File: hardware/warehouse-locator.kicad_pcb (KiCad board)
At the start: 2 copper layers, 8 parts, among them J1 Screw_Terminal_01x03, J2 Screw_Terminal_01x03, J3 Screw_Terminal_01x03, J4 Barrel_Jack, J5 Screw_Terminal_01x03, J6 Screw_Terminal_01x03, J7 Screw_Terminal_01x03, U1 ESP32-DevKitC

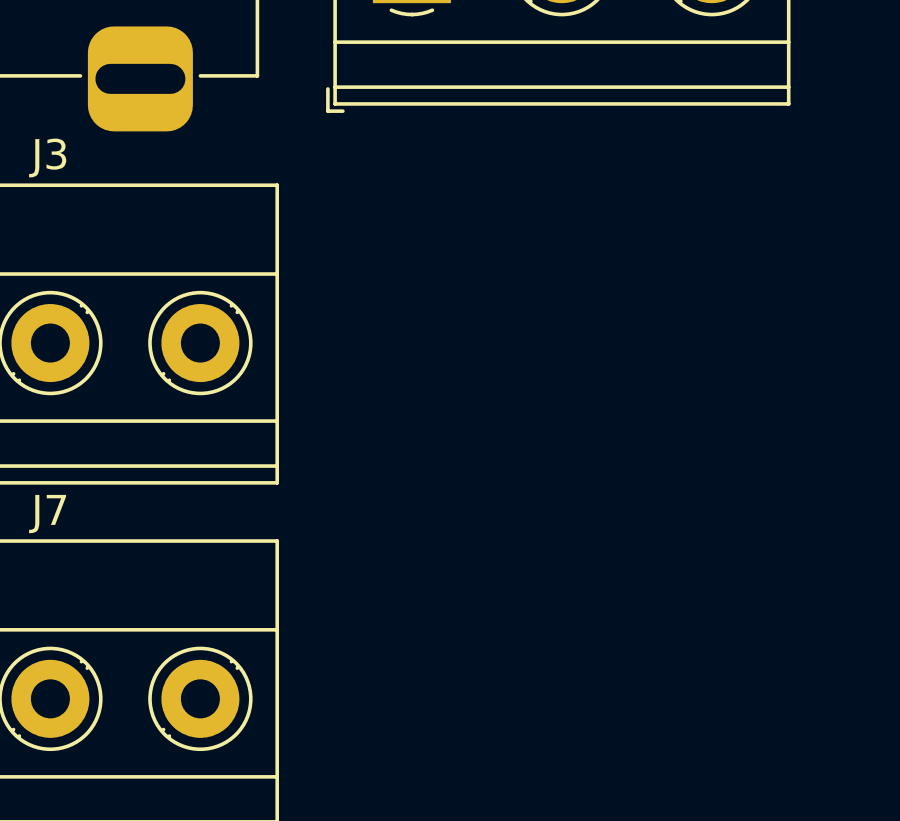
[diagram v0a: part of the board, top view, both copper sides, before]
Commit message: Ethernet header
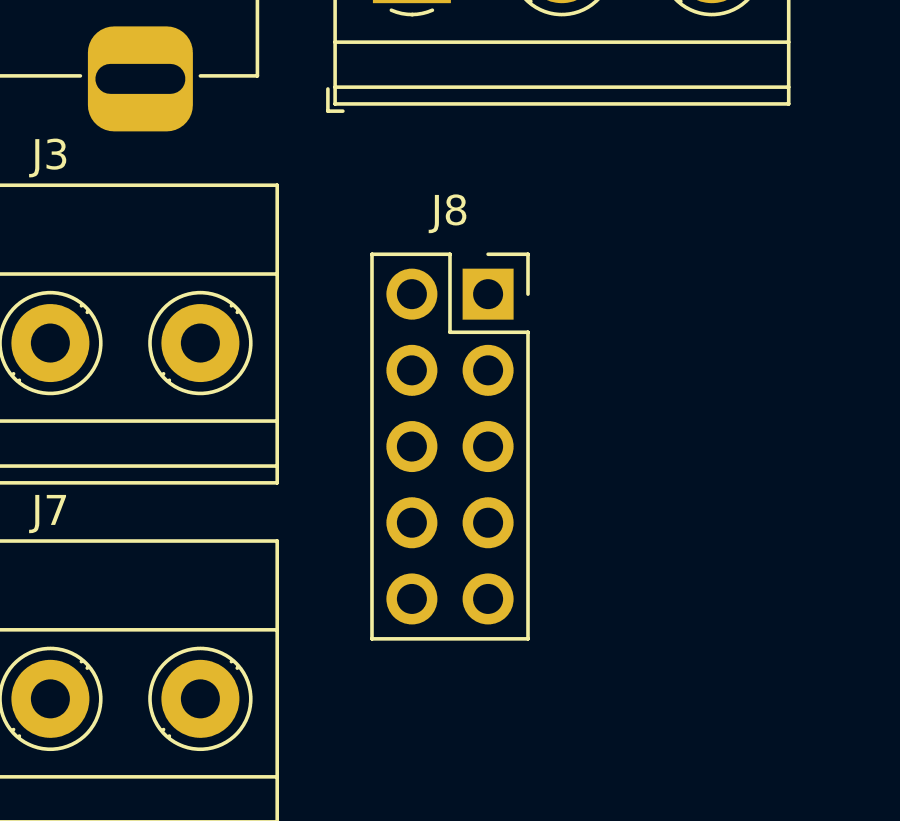
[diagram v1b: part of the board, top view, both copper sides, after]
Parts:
- added J8: Ethernet, Connector_PinSocket_2.54mm:PinSocket_2x05_P2.54mm_Vertical, F.Cu at (170.2, 86.4)
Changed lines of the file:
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@@
   (net 45 "unconnected-(U1-Pad37)")
   (net 46 "unconnected-(U1-Pad38)")
+  (net 47 "unconnected-(J8-Pad1)")
+  (net 48 "unconnected-(J8-Pad2)")
+  (net 49 "unconnected-(J8-Pad3)")
+  (net 50 "/CIPO")
+  (net 51 "/COPI")
+  (net 52 "/SCLK")
+  (net 53 "/ETH_CS")
+  (net 54 "/ETH_RESET")
+  (net 55 "+3.3V")
   (footprint "Espressif:ESP32-DevKitC" (layer "F.Cu")
     (at 119.605 64.83812)
@@
       (offset (xyz 0 0 0))
       (scale (xyz 1 1 1))
+      (rotate (xyz 0 0 0))
+    )
+  )
+  (footprint "Connector_PinSocket_2.54mm:PinSocket_2x05_P2.54mm_Vertical" (layer "F.Cu")
+    (at 170.18 86.36)
+    (descr "Through hole straight socket strip, 2x05, 2.54mm pitch, double cols (from Kicad 4.0.7), script generated")
+    (tags "Through hole socket strip THT 2x05 2.54mm double row")
+    (property "Sheetfile" "warehouse-locator.kicad_sch")
+    (property "Sheetname" "")
+    (attr through_hole)
+    (fp_text reference "J8" (at -1.27 -2.77) (layer "F.SilkS")
+      (effects (font (size 1 1) (thickness 0.15)))
+    )
+    (fp_text value "Ethernet" (at -1.27 12.93) (layer "F.Fab")
+      (effects (font (size 1 1) (thickness 0.15)))
+    )
+    (fp_text user "${REFERENCE}" (at -1.27 5.08 90) (layer "F.Fab")
+      (effects (font (size 1 1) (thickness 0.15)))
+    )
+    (fp_line (start 0 -1.33) (end 1.33 -1.33) (layer "F.SilkS") (width 0.12))
+    (fp_line (start -1.27 1.27) (end 1.33 1.27) (layer "F.SilkS") (width 0.12))
+    (fp_line (start 1.33 1.27) (end 1.33 11.49) (layer "F.SilkS") (width 0.12))
+    (fp_line (start -3.87 -1.33) (end -1.27 -1.33) (layer "F.SilkS") (width 0.12))
+    (fp_line (start -3.87 11.49) (end 1.33 11.49) (layer "F.SilkS") (width 0.12))
+    (fp_line (start -3.87 -1.33) (end -3.87 11.49) (layer "F.SilkS") (width 0.12))
+    (fp_line (start -1.27 -1.33) (end -1.27 1.27) (layer "F.SilkS") (width 0.12))
+    (fp_line (start 1.33 -1.33) (end 1.33 0) (layer "F.SilkS") (width 0.12))
+    (fp_line (start 1.76 -1.8) (end 1.76 11.9) (layer "F.CrtYd") (width 0.05))
+    (fp_line (start 1.76 11.9) (end -4.34 11.9) (layer "F.CrtYd") (width 0.05))
+    (fp_line (start -4.34 11.9) (end -4.34 -1.8) (layer "F.CrtYd") (width 0.05))
+    (fp_line (start -4.34 -1.8) (end 1.76 -1.8) (layer "F.CrtYd") (width 0.05))
+    (fp_line (start -3.81 -1.27) (end 0.27 -1.27) (layer "F.Fab") (width 0.1))
+    (fp_line (start 1.27 11.43) (end -3.81 11.43) (layer "F.Fab") (width 0.1))
+    (fp_line (start 1.27 -0.27) (end 1.27 11.43) (layer "F.Fab") (width 0.1))
+    (fp_line (start -3.81 11.43) (end -3.81 -1.27) (layer "F.Fab") (width 0.1))
+    (fp_line (start 0.27 -1.27) (end 1.27 -0.27) (layer "F.Fab") (width 0.1))
+    (pad "1" thru_hole rect (at 0 0) (size 1.7 1.7) (drill 1) (layers *.Cu *.Mask)
+      (net 47 "unconnected-(J8-Pad1)") (pinfunction "Pin_1") (pintype "passive+no_connect"))
+    (pad "2" thru_hole oval (at -2.54 0) (size 1.7 1.7) (drill 1) (layers *.Cu *.Mask)
+      (net 48 "unconnected-(J8-Pad2)") (pinfunction "Pin_2") (pintype "passive+no_connect"))
+    (pad "3" thru_hole oval (at 0 2.54) (size 1.7 1.7) (drill 1) (layers *.Cu *.Mask)
+      (net 49 "unconnected-(J8-Pad3)") (pinfunction "Pin_3") (pintype "passive+no_connect"))
+    (pad "4" thru_hole oval (at -2.54 2.54) (size 1.7 1.7) (drill 1) (layers *.Cu *.Mask)
+      (net 50 "/CIPO") (pinfunction "Pin_4") (pintype "passive"))
+    (pad "5" thru_hole oval (at 0 5.08) (size 1.7 1.7) (drill 1) (layers *.Cu *.Mask)
+      (net 51 "/COPI") (pinfunction "Pin_5") (pintype "passive"))
+    (pad "6" thru_hole oval (at -2.54 5.08) (size 1.7 1.7) (drill 1) (layers *.Cu *.Mask)
+      (net 52 "/SCLK") (pinfunction "Pin_6") (pintype "passive"))
+    (pad "7" thru_hole oval (at 0 7.62) (size 1.7 1.7) (drill 1) (layers *.Cu *.Mask)
+      (net 53 "/ETH_CS") (pinfunction "Pin_7") (pintype "passive"))
+    (pad "8" thru_hole oval (at -2.54 7.62) (size 1.7 1.7) (drill 1) (layers *.Cu *.Mask)
+      (net 54 "/ETH_RESET") (pinfunction "Pin_8") (pintype "passive"))
+    (pad "9" thru_hole oval (at 0 10.16) (size 1.7 1.7) (drill 1) (layers *.Cu *.Mask)
+      (net 55 "+3.3V") (pinfunction "Pin_9") (pintype "passive"))
+    (pad "10" thru_hole oval (at -2.54 10.16) (size 1.7 1.7) (drill 1) (layers *.Cu *.Mask)
+      (net 3 "GND") (pinfunction "Pin_10") (pintype "passive"))
+    (model "${KICAD6_3DMODEL_DIR}/Connector_PinSocket_2.54mm.3dshapes/PinSocket_2x05_P2.54mm_Vertical.wrl"
+      (offset (xyz 0 0 0))
+      (scale (xyz 1 1 1))

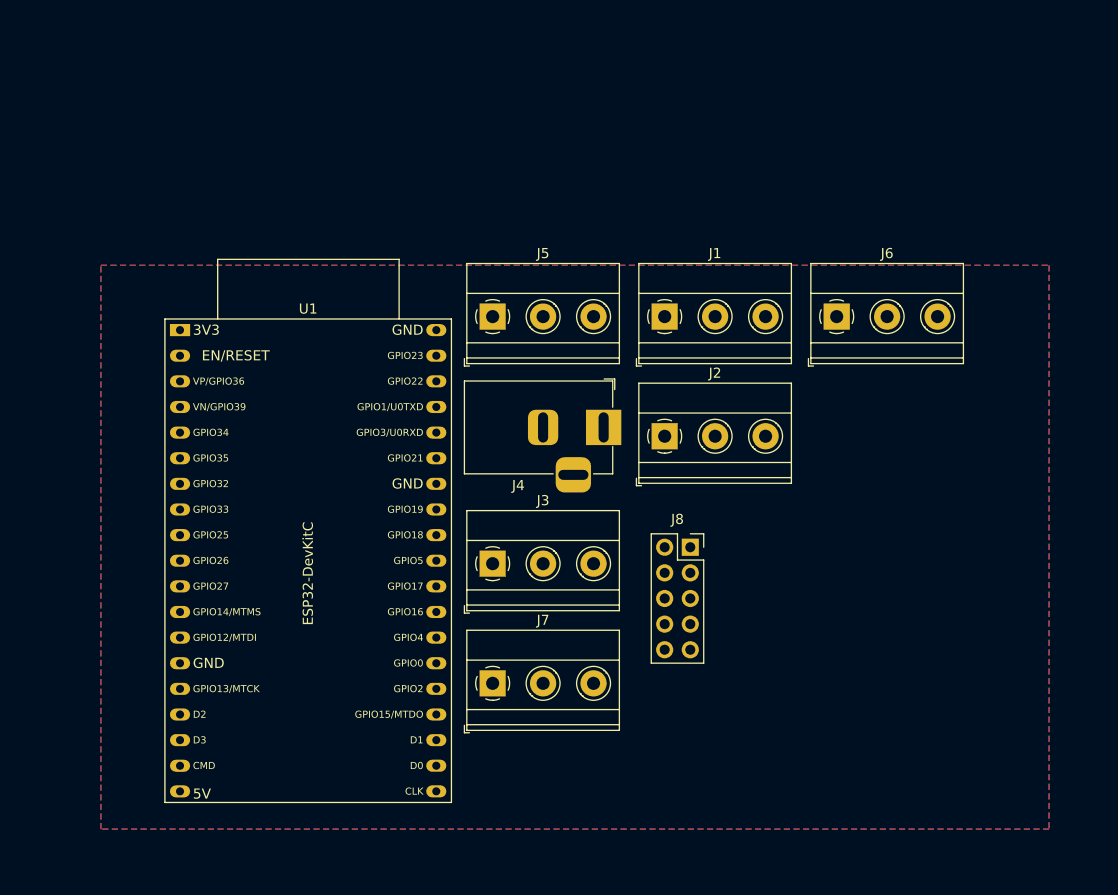
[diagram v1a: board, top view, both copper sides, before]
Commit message: Component positioning
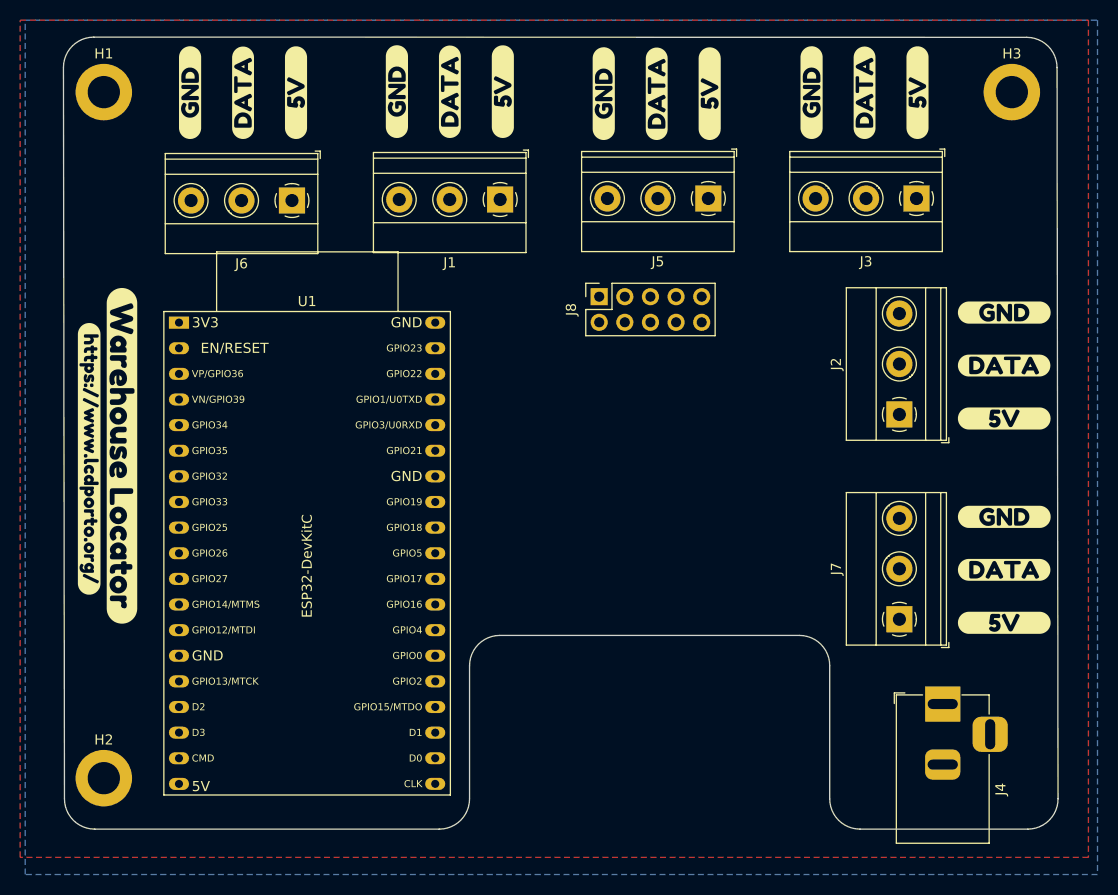
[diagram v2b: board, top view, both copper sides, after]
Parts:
- added H1: MountingHole, MountingHole:MountingHole_3.2mm_M3_DIN965_Pad, F.Cu at (112.0, 41.2)
- added H2: MountingHole, MountingHole:MountingHole_3.2mm_M3_DIN965_Pad, F.Cu at (112.0, 109.2)
- added H3: MountingHole, MountingHole:MountingHole_3.2mm_M3_DIN965_Pad, F.Cu at (202.1, 41.2)
- added kibuzzard-63B4CA0A: G***, kibuzzard-63B4CA0A, F.Cu at (201.3, 88.6)
- added kibuzzard-63B4CA0A: G***, kibuzzard-63B4CA0A, F.Cu at (125.9, 41.3)
- added kibuzzard-63B4CA0A: G***, kibuzzard-63B4CA0A, F.Cu at (187.5, 41.3)
- added kibuzzard-63B4CA0A: G***, kibuzzard-63B4CA0A, F.Cu at (201.3, 68.4)
- added kibuzzard-63B4CA0A: G***, kibuzzard-63B4CA0A, F.Cu at (166.9, 41.4)
- added kibuzzard-63B4CA0A: G***, kibuzzard-63B4CA0A, F.Cu at (146.4, 41.2)
- added kibuzzard-63B4CA0E: G***, kibuzzard-63B4CA0E, F.Cu at (151.6, 41.2)
- added kibuzzard-63B4CA0E: G***, kibuzzard-63B4CA0E, F.Cu at (201.3, 93.8)
- added kibuzzard-63B4CA0E: G***, kibuzzard-63B4CA0E, F.Cu at (192.7, 41.3)
- added kibuzzard-63B4CA0E: G***, kibuzzard-63B4CA0E, F.Cu at (201.3, 73.6)
- added kibuzzard-63B4CA0E: G***, kibuzzard-63B4CA0E, F.Cu at (172.1, 41.4)
- added kibuzzard-63B4CA0E: G***, kibuzzard-63B4CA0E, F.Cu at (131.1, 41.3)
- added kibuzzard-63B4CA19: G***, kibuzzard-63B4CA19, F.Cu at (120.6, 41.3)
- added kibuzzard-63B4CA19: G***, kibuzzard-63B4CA19, F.Cu at (182.2, 41.3)
- added kibuzzard-63B4CA19: G***, kibuzzard-63B4CA19, F.Cu at (141.1, 41.2)
- added kibuzzard-63B4CA19: G***, kibuzzard-63B4CA19, F.Cu at (201.3, 83.3)
- added kibuzzard-63B4CA19: G***, kibuzzard-63B4CA19, F.Cu at (161.6, 41.4)
- added kibuzzard-63B4CA19: G***, kibuzzard-63B4CA19, F.Cu at (201.3, 63.1)
- added kibuzzard-63B4CBD0: G***, kibuzzard-63B4CBD0, F.Cu at (113.8, 77.3)
- added kibuzzard-63B4CC08: G***, kibuzzard-63B4CC08, F.Cu at (110.6, 77.6)
- moved J3 55.5 mm to (192.6, 51.8), turned to 180 degrees
- moved J6 55.2 mm to (130.7, 52.0), turned to 180 degrees
- moved J4 43.4 mm to (195.2, 101.9), turned to 90 degrees
- moved J7 40.8 mm to (190.9, 93.5), turned to 90 degrees
- moved J8 26.4 mm to (161.2, 61.5), turned to 90 degrees
- moved J5 24.4 mm to (172.0, 51.8), turned to 180 degrees
- moved J2 23.4 mm to (190.9, 73.2), turned to 90 degrees
- moved J1 20.0 mm to (151.3, 51.9), turned to 180 degrees
- moved U1 0.75 mm to (119.5, 64.1)
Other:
- board outline added: 98.6 x 78.5 mm

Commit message: Pins connected
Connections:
- J8 pad 8: /ETH_RESET -> unconnected-(J8-Pad8)
- U1 pad 1: unconnected-(U1-Pad1) -> +3.3V
- U1 pad 14: unconnected-(U1-Pad14) -> GND
- U1 pad 19: unconnected-(U1-Pad19) -> +5V
- U1 pad 24: unconnected-(U1-Pad24) -> /LED5
- U1 pad 26: unconnected-(U1-Pad26) -> /LED2
- U1 pad 27: unconnected-(U1-Pad27) -> /LED4
- U1 pad 28: unconnected-(U1-Pad28) -> /LED1
- U1 pad 29: unconnected-(U1-Pad29) -> /ETH_CS
- U1 pad 30: unconnected-(U1-Pad30) -> /SCLK
- U1 pad 31: unconnected-(U1-Pad31) -> /CIPO
- U1 pad 32: unconnected-(U1-Pad32) -> GND
- U1 pad 33: unconnected-(U1-Pad33) -> /LED0
- U1 pad 36: unconnected-(U1-Pad36) -> /LED3
- U1 pad 37: unconnected-(U1-Pad37) -> /COPI
- U1 pad 38: unconnected-(U1-Pad38) -> GND

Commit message: Board routed
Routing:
- net /LED4: track 0.00 -> 61.2 mm
- net +3.3V: track 0.00 -> 59.1 mm
- net /LED2: track 0.00 -> 56.9 mm
- net /LED5: track 0.00 -> 52.5 mm
- net /LED1: track 0.00 -> 46.8 mm
- net /LED3: track 0.00 -> 41.8 mm
- net /ETH_CS: track 0.00 -> 39.0 mm
- net /SCLK: track 0.00 -> 33.2 mm
- net /LED0: track 0.00 -> 32.9 mm
- net /CIPO: track 0.00 -> 29.2 mm
- net /COPI: track 0.00 -> 26.2 mm
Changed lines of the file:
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@@
   (gr_line (start 111.15 114.3) (end 145.3 114.3) (layer "Edge.Cuts") (width 0.1))
   (gr_line (start 181 95.1) (end 151.3 95.1) (layer "Edge.Cuts") (width 0.1))
+  (segment (start 148.40344 76.79656) (end 144.9 76.79656) (width 0.25) (layer "B.Cu") (net 2))
+  (segment (start 146.333334 51.895) (end 146.333334 54.733334) (width 0.25) (layer "B.Cu") (net 2))
+  (segment (start 152.8 61.2) (end 152.8 72.4) (width 0.25) (layer "B.Cu") (net 2))
+  (segment (start 146.333334 54.733334) (end 152.8 61.2) (width 0.25) (layer "B.Cu") (net 2))
+  (segment (start 152.8 72.4) (end 148.40344 76.79656) (width 0.25) (layer "B.Cu") (net 2))
+  (segment (start 147.42344 94.57656) (end 144.9 94.57656) (width 0.25) (layer "B.Cu") (net 4))
+  (segment (start 190.905 68.2) (end 176.5 68.2) (width 0.25) (layer "B.Cu") (net 4))
+  (segment (start 151.85 92.85) (end 149.15 92.85) (width 0.25) (layer "B.Cu") (net 4))
+  (segment (start 176.5 68.2) (end 151.85 92.85) (width 0.25) (layer "B.Cu") (net 4))
+  (segment (start 149.15 92.85) (end 147.42344 94.57656) (width 0.25) (layer "B.Cu") (net 4))
+  (segment (start 150.41344 92.03656) (end 144.9 92.03656) (width 0.25) (layer "B.Cu") (net 5))
+  (segment (start 187.6 54.85) (end 150.41344 92.03656) (width 0.25) (layer "B.Cu") (net 5))
+  (segment (start 187.6 51.795) (end 187.6 54.85) (width 0.25) (layer "B.Cu") (net 5))
+  (segment (start 159.45 74.94656) (end 144.9 89.49656) (width 0.25) (layer "B.Cu") (net 6))
+  (segment (start 166.966667 51.795) (end 159.45 59.311667) (width 0.25) (layer "B.Cu") (net 6))
+  (segment (start 159.45 59.311667) (end 159.45 74.94656) (width 0.25) (layer "B.Cu") (net 6))
+  (segment (start 130.45 60.05) (end 148.25 60.05) (width 0.25) (layer "B.Cu") (net 7))
+  (segment (start 150.2 67) (end 148.02344 69.17656) (width 0.25) (layer "B.Cu") (net 7))
+  (segment (start 148.02344 69.17656) (end 144.9 69.17656) (width 0.25) (layer "B.Cu") (net 7))
+  (segment (start 125.7 55.3) (end 130.45 60.05) (width 0.25) (layer "B.Cu") (net 7))
+  (segment (start 125.7 51.995) (end 125.7 55.3) (width 0.25) (layer "B.Cu") (net 7))
+  (segment (start 150.2 62) (end 150.2 67) (width 0.25) (layer "B.Cu") (net 7))
+  (segment (start 148.25 60.05) (end 150.2 62) (width 0.25) (layer "B.Cu") (net 7))
+  (segment (start 149.35 93.95) (end 147.1 96.2) (width 0.25) (layer "B.Cu") (net 8))
+  (segment (start 147.1 96.2) (end 147.1 99.35) (width 0.25) (layer "B.Cu") (net 8))
+  (segment (start 190.905 88.5) (end 157.5 88.5) (width 0.25) (layer "B.Cu") (net 8))
+  (segment (start 157.5 88.5) (end 152.05 93.95) (width 0.25) (layer "B.Cu") (net 8))
+  (segment (start 146.79344 99.65656) (end 144.9 99.65656) (width 0.25) (layer "B.Cu") (net 8))
+  (segment (start 152.05 93.95) (end 149.35 93.95) (width 0.25) (layer "B.Cu") (net 8))
+  (segment (start 147.1 99.35) (end 146.79344 99.65656) (width 0.25) (layer "B.Cu") (net 8))
+  (segment (start 163.69 69.26) (end 151.07344 81.87656) (width 0.25) (layer "F.Cu") (net 36))
+  (segment (start 163.69 64.066) (end 163.69 69.26) (width 0.25) (layer "F.Cu") (net 36))
+  (segment (start 151.07344 81.87656) (end 144.9 81.87656) (width 0.25) (layer "F.Cu") (net 36))
+  (segment (start 147.11344 66.63656) (end 144.9 66.63656) (width 0.25) (layer "F.Cu") (net 37))
+  (segment (start 166.23 61.526) (end 166.23 59.93) (width 0.25) (layer "F.Cu") (net 37))
+  (segment (start 166.23 59.93) (end 165.6 59.3) (width 0.25) (layer "F.Cu") (net 37))
+  (segment (start 154.45 59.3) (end 147.11344 66.63656) (width 0.25) (layer "F.Cu") (net 37))
+  (segment (start 165.6 59.3) (end 154.45 59.3) (width 0.25) (layer "F.Cu") (net 37))
+  (segment (start 151.83344 84.41656) (end 144.9 84.41656) (width 0.25) (layer "F.Cu") (net 38))
+  (segment (start 166.23 70.02) (end 151.83344 84.41656) (width 0.25) (layer "F.Cu") (net 38))
+  (segment (start 166.23 64.066) (end 166.23 70.02) (width 0.25) (layer "F.Cu") (net 38))
+  (segment (start 167.595 62.701) (end 167.595 70.505) (width 0.25) (layer "F.Cu") (net 39))
+  (segment (start 168.77 61.526) (end 167.595 62.701) (width 0.25) (layer "F.Cu") (net 39))
+  (segment (start 151.14344 86.95656) (end 144.9 86.95656) (width 0.25) (layer "F.Cu") (net 39))
+  (segment (start 167.595 70.505) (end 151.14344 86.95656) (width 0.25) (layer "F.Cu") (net 39))
+  (segment (start 122.8 57.65) (end 119.5 60.95) (width 0.25) (layer "F.Cu") (net 40))
+  (segment (start 171.31 59.51) (end 169.45 57.65) (width 0.25) (layer "F.Cu") (net 40))
+  (segment (start 171.31 61.526) (end 171.31 59.51) (width 0.25) (layer "F.Cu") (net 40))
+  (segment (start 119.5 60.95) (end 119.5 64.09656) (width 0.25) (layer "F.Cu") (net 40))
+  (segment (start 169.45 57.65) (end 122.8 57.65) (width 0.25) (layer "F.Cu") (net 40))
   (zone (net 3) (net_name "GND") (layer "F.Cu") (hatch edge 0.508)
     (connect_pads (clearance 0.508))

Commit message: Add Status LED
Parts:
- added D1: LED, LED_THT:LED_D5.0mm, F.Cu at (111.5, 99.7)
- added R1: 220, Resistor_THT:R_Axial_DIN0207_L6.3mm_D2.5mm_P10.16mm_Horizontal, F.Cu at (137.5, 104.8)
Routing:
- net Net-(D1-Pad2): track 0.00 -> 15.4 mm
